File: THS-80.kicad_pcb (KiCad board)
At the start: 4 copper layers, 101.6 x 101.6 mm, 104 parts, among them J1 USB_B_Micro, J10 CTC Header, J2 RC80 Bus, J3 RC80 Expansion, J4 IDE, J5 JTAG, J6 PMOD, J7 PIO Header, J8 Port B, J9 Port A, Q1 IRLML6402, Q2 IRLML6402, SW1 Reset, SW2 SW_DIP_x06, U1 MAX40203AUK, U2 DS1813R-5+T&R, U3 EPM7064STC100, U4 Z84C0010AEG, U5 IS62C5128BL-45TLI, U6 SST39SF040, U7 Z84C2010AEG, U8 Z84C4310AEG, U9 Z84C3010AEG, X1 CFPS-72 50mhz

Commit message: more routing
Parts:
- C1, C14, C15, C2, C22, C23, C3, C4, D12, D3, Q1, Q2, R1, R13, R14, R15, R19, R20, R23, R35, R36, R37, R38, R7, R8, R9, U1: moved to F.Cu
- C18: moved to B.Cu
- moved C22 84.0 mm to (112.1, 33.9), turned to 0 degrees
- moved C4 36.2 mm to (180.6, 36.8), turned to 90 degrees
- moved C18 9.53 mm to (150.7, 51.4), turned to 270 degrees
- moved R15 3.54 mm to (118.4, 90.2), turned to 180 degrees
- moved R20 3.43 mm to (149.6, 66.7), turned to 180 degrees
- moved R19 1.35 mm to (149.6, 68.2), turned to 180 degrees
- moved C9 1.14 mm to (151.9, 92.7)
- moved C15 0.76 mm to (111.9, 76.2)
- moved D12 0.65 mm to (111.8, 79.9)
- moved C14 0.64 mm to (106.7, 86.4)
- moved D3 0.64 mm to (111.8, 72.4)
- moved C17 0.63 mm to (184.8, 45.1)
- turned Q1 to 0 degrees
- turned Q2 to 0 degrees
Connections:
- D10 pad 1: /CPLD/LED6 -> /CPLD/LED1
- D11 pad 1: /CPLD/LED7 -> /CPLD/LED0
- D4 pad 1: /CPLD/LED0 -> /CPLD/LED7
- D5 pad 1: /CPLD/LED1 -> /CPLD/LED6
- D6 pad 1: /CPLD/LED2 -> /CPLD/LED5
- D7 pad 1: /CPLD/LED3 -> /CPLD/LED4
- D8 pad 1: /CPLD/LED4 -> /CPLD/LED3
- D9 pad 1: /CPLD/LED5 -> /CPLD/LED2
- J7 pad 10: /Peripherals/PB4 -> /Peripherals/PB1
- J7 pad 11: /Peripherals/PA3 -> /Peripherals/PA2
- J7 pad 12: /Peripherals/PB3 -> /Peripherals/PB2
- J7 pad 13: /Peripherals/PA2 -> /Peripherals/PA3
- J7 pad 14: /Peripherals/PB2 -> /Peripherals/PB3
- J7 pad 15: /Peripherals/PA1 -> /Peripherals/PA4
- J7 pad 16: /Peripherals/PB1 -> /Peripherals/PB4
- J7 pad 17: /Peripherals/PA0 -> /Peripherals/PA5
- J7 pad 18: /Peripherals/PB0 -> /Peripherals/PB5
- J7 pad 19: /Peripherals/ARDY -> /Peripherals/PA6
- J7 pad 20: /Peripherals/BRDY -> /Peripherals/PB6
- J7 pad 21: /Peripherals/~ASTB -> /Peripherals/PA7
- J7 pad 22: /Peripherals/~BSTB -> /Peripherals/PB7
- J7 pad 3: /Peripherals/PA7 -> /Peripherals/~ASTB
- J7 pad 4: /Peripherals/PB7 -> /Peripherals/~BSTB
- J7 pad 5: /Peripherals/PA6 -> /Peripherals/ARDY
- J7 pad 6: /Peripherals/PB6 -> /Peripherals/BRDY
- J7 pad 7: /Peripherals/PA5 -> /Peripherals/PA0
- J7 pad 8: /Peripherals/PB5 -> /Peripherals/PB0
- J7 pad 9: /Peripherals/PA4 -> /Peripherals/PA1
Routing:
- net /~RESET: track 24.0 -> 239.1 mm, vias 2 -> 10
- net /~RD: track 58.8 -> 237.5 mm, vias 2 -> 11
- net /A1: track 109.3 -> 253.7 mm, vias 5 -> 15
- net /D7: track 133.5 -> 259.8 mm, vias 9 -> 17
- net VCC: track 21.6 -> 145.5 mm, vias 0 -> 49
- net /~WR: track 29.0 -> 149.0 mm, vias 2 -> 7
- net /D1: track 127.6 -> 243.6 mm, vias 9 -> 13
- net GND: track 19.4 -> 126.7 mm, vias 0 -> 47
- net /D6: track 164.5 -> 265.5 mm, vias 8 -> 15
- net /CLK_U: track 0.00 -> 98.7 mm, vias 0 -> 4
- net /D5: track 175.8 -> 272.7 mm, vias 14 -> 19
- net /Peripherals/CLK_A: track 0.00 -> 93.1 mm, vias 0 -> 4
- net /CLK_CPU: track 0.00 -> 92.6 mm, vias 0 -> 9
- net /D0: track 149.9 -> 240.6 mm, vias 8 -> 13
- net /~IORQ: track 59.4 -> 146.4 mm, vias 3 -> 9
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
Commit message: almost there...
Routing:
- net /CPLD/PMOD3: track 0.00 -> 61.5 mm, vias 0 -> 4
- net /CPLD/SW4: track 4.84 -> 65.4 mm, vias 0 -> 4
- net /CPLD/PMOD5: track 0.00 -> 57.6 mm, vias 0 -> 4
- net /CPLD/PMOD4: track 0.00 -> 56.5 mm, vias 0 -> 4
- net /CPLD/PMOD6: track 0.00 -> 55.2 mm, vias 0 -> 4
- net /CPLD/PMOD7: track 0.00 -> 53.5 mm, vias 0 -> 4
- net /CPLD/LED7: track 0.00 -> 48.9 mm, vias 0 -> 3
- net /CPLD/SW3: track 29.5 -> 59.0 mm, vias 2 -> 5
- net /A1: track 253.7 -> 256.7 mm
- net /D1: track 243.6 -> 244.7 mm
- net GND: track 126.7 -> 127.5 mm
- net /D3: track 253.2 -> 252.5 mm
- net /CPLD/SW0: track 44.6 -> 45.3 mm
- net /~RD: track 237.5 -> 238.2 mm
- net /CPLD/TCK: track 61.5 -> 62.1 mm

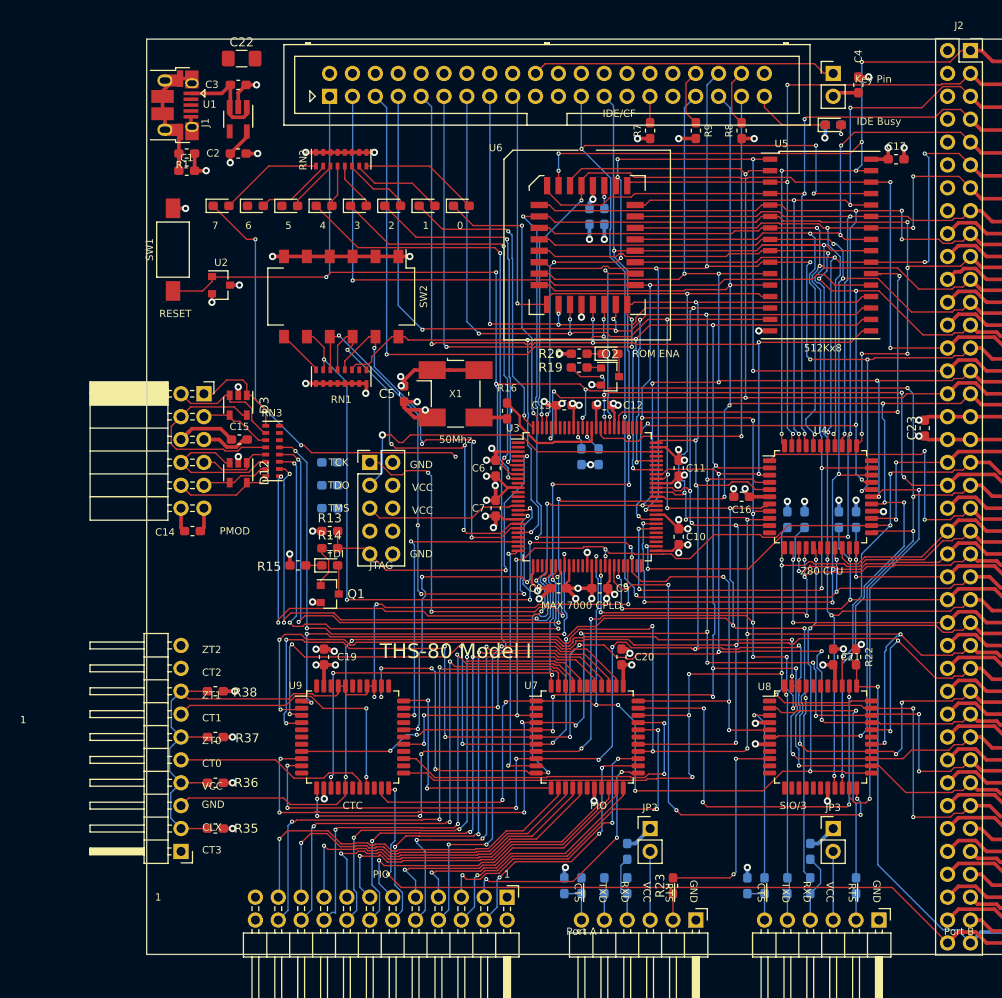
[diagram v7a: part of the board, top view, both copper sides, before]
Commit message: finished routing, passed DRC
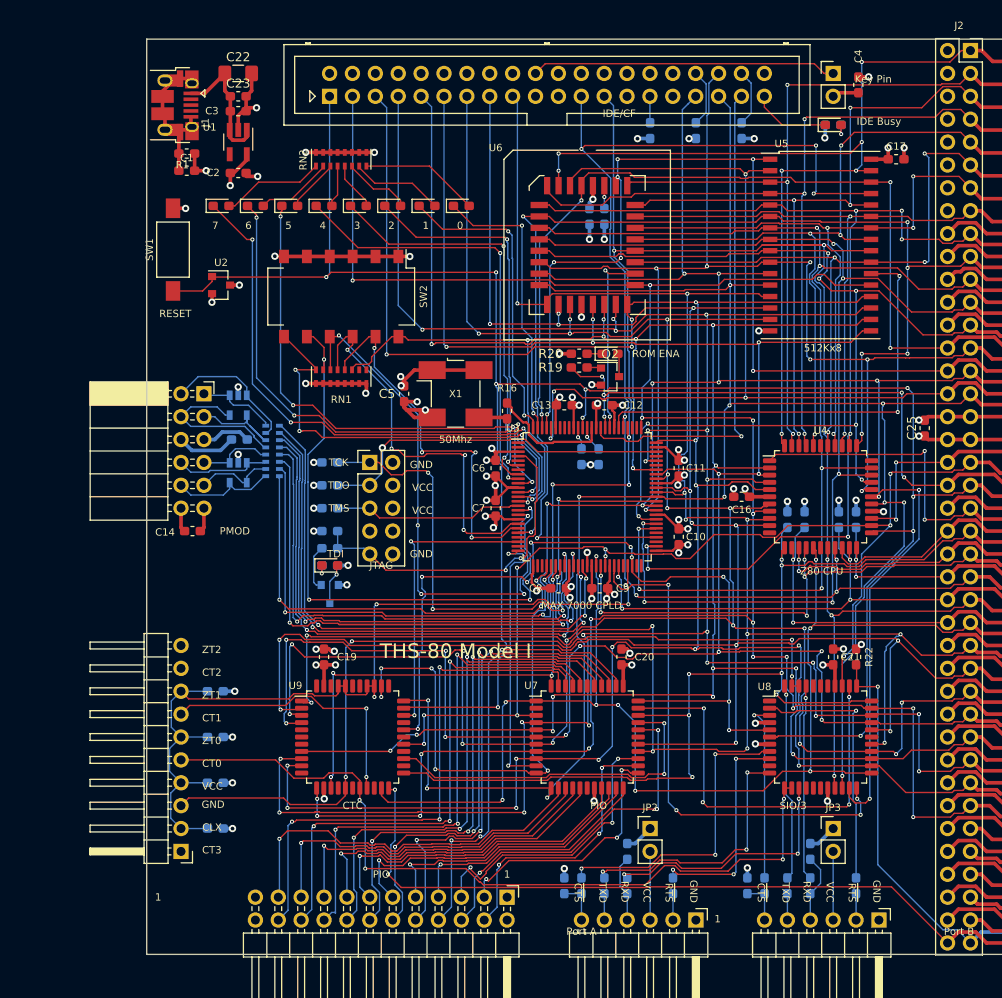
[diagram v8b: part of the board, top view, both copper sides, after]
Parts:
- added C25: 100nF, Capacitor_SMD:C_0603_1608Metric_Pad1.05x0.95mm_HandSolder, F.Cu at (188.0, 74.9)
- C15, D12, D3, Q1, R13, R14, R15, R23, R35, R36, R37, R38, R7, R8, R9, RN3: moved to B.Cu
- C3: value .33uF -> 2.2uF
- moved C23 84.6 mm to (111.8, 38.1), turned to 0 degrees
- moved R15 3.54 mm to (121.9, 90.2), turned to 0 degrees
- moved C3 2.92 mm to (111.8, 39.8)
- moved U1 2.54 mm to (111.8, 43.2)
- moved C2 2.16 mm to (111.8, 46.6)
- moved C22 1.69 mm to (111.8, 35.6)
- turned Q1 to 270 degrees
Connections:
- C22 pad 1: VCC -> Net-(C22-Pad1)
- C23 pad 1: VCC -> Net-(C22-Pad1)
- C3 pad 1: Net-(C3-Pad1) -> Net-(C22-Pad1)
- J1 pad 1: Net-(C3-Pad1) -> Net-(C22-Pad1)
- RN3 pad 1: /CPLD/R0 -> /CPLD/R7
- RN3 pad 10: /CPLD/PMOD6 -> /CPLD/PMOD1
- RN3 pad 11: /CPLD/PMOD5 -> /CPLD/PMOD2
- RN3 pad 12: /CPLD/PMOD4 -> /CPLD/PMOD3
- RN3 pad 13: /CPLD/PMOD3 -> /CPLD/PMOD4
- RN3 pad 14: /CPLD/PMOD2 -> /CPLD/PMOD5
- RN3 pad 15: /CPLD/PMOD1 -> /CPLD/PMOD6
- RN3 pad 16: /CPLD/PMOD0 -> /CPLD/PMOD7
- RN3 pad 2: /CPLD/R1 -> /CPLD/R6
- RN3 pad 3: /CPLD/R2 -> /CPLD/R5
- RN3 pad 4: /CPLD/R3 -> /CPLD/R4
- RN3 pad 5: /CPLD/R4 -> /CPLD/R3
- RN3 pad 6: /CPLD/R5 -> /CPLD/R2
- RN3 pad 7: /CPLD/R6 -> /CPLD/R1
- RN3 pad 8: /CPLD/R7 -> /CPLD/R0
- RN3 pad 9: /CPLD/PMOD7 -> /CPLD/PMOD0
- U1 pad 1: Net-(C3-Pad1) -> Net-(C22-Pad1)
- U1 pad 3: Net-(C3-Pad1) -> Net-(C22-Pad1)
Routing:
- net /Peripherals/CLK_B: track 22.1 -> 88.9 mm, vias 0 -> 4
- net /CPLD/LED6: track 0.00 -> 61.7 mm, vias 0 -> 4
- net /CPLD/PMOD2: track 0.00 -> 61.4 mm, vias 0 -> 3
- net /CPLD/PMOD1: track 0.00 -> 60.8 mm, vias 0 -> 3
- net /CPLD/PMOD0: track 0.00 -> 60.2 mm, vias 0 -> 3
- net /CPLD/LED5: track 0.00 -> 56.9 mm, vias 0 -> 4
- net /A0: track 190.8 -> 236.2 mm, vias 9 -> 11
- net /CPLD/SW5: track 5.17 -> 49.7 mm, vias 0 -> 4
- net /Peripherals/~CTSB: track 0.00 -> 33.8 mm, vias 0 -> 3
- net /Peripherals/TXB: track 0.00 -> 29.1 mm, vias 0 -> 3
- net /Peripherals/RXB: track 0.00 -> 28.6 mm, vias 0 -> 3
- net /CPLD/PMOD5: track 57.6 -> 81.5 mm, vias 4 -> 3
- net /CPLD/LED7: track 48.9 -> 65.6 mm, vias 3 -> 4
- net Net-(C22-Pad1): track 0.00 -> 15.4 mm
- net Net-(C3-Pad1): track 11.0 -> 0.00 mm
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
